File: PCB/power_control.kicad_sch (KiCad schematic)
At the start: 12 parts

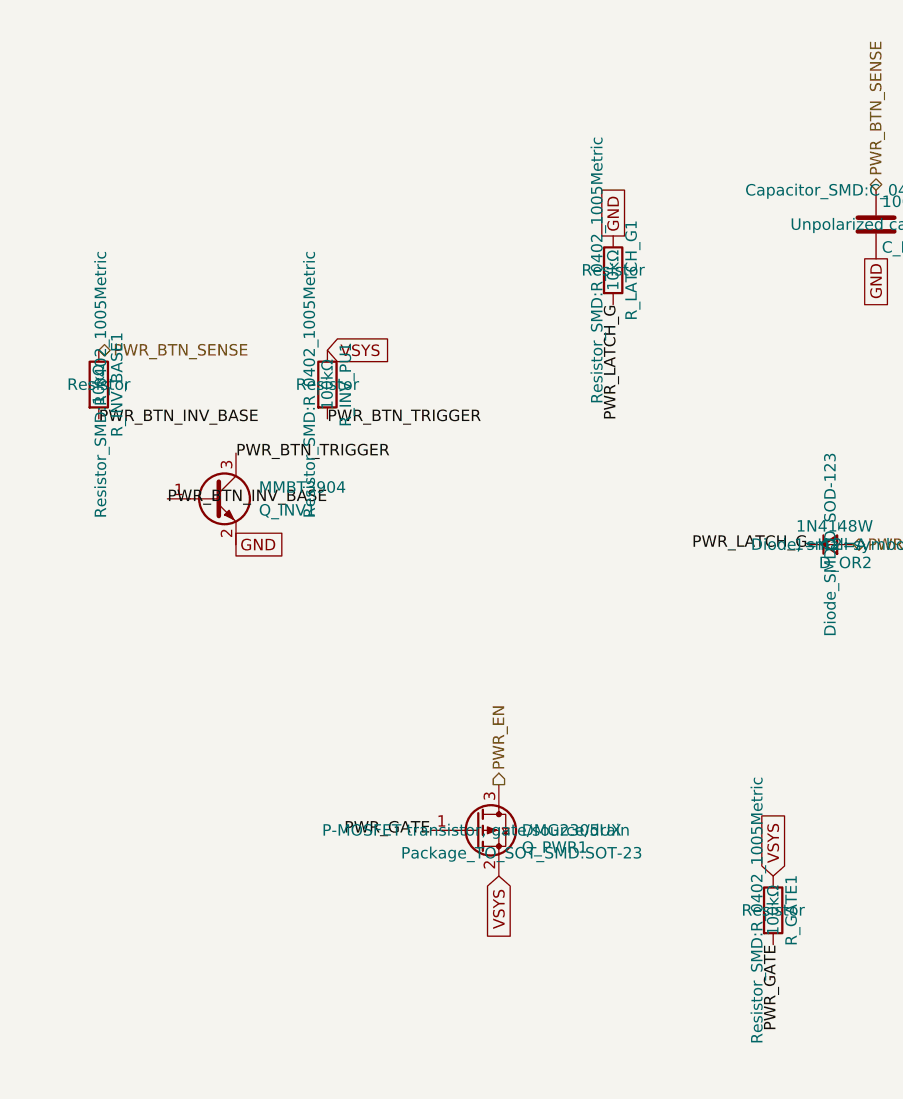
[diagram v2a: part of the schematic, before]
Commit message: fix: latch gate-drive divider, floating buck EN, and missing accelerometer MPNs (#58)
Power latch, round 2 (found via cross-checking a third-party static-analysis
tool run against this project's own netlist and real component datasheets):

- R_LATCH_G1 raised 10kΩ -> 1MΩ. The prior value formed an unintended divider
  with R_INV_PU1 across D_OR1, leaving only ~0.3V at Q_LATCH1's gate on a
  press -- nowhere near enough to turn it on, meaning last round's inverter
  fix likely didn't actually latch on real hardware. Raising the pull-down
  instead of shrinking the pull-up avoids turning Q_INV1's idle state into a
  continuous mA-scale drain.
- R_INV_BASE1 repurposed from a series resistor (which shared current with
  R_BTN_PU1 and sagged the MCU's own button-sense read to ~1V) into its own
  dedicated 100k VSYS pull-up, decoupled via a new Schottky (D_INV_ISO1,
  BAT54W) so a press can still pull the base low without loading the shared
  sense node.
- Added R_PWR_EN_PD1 (100k to GND): the buck's EN pin had no pull-up or
  pull-down at all. TI's TLV62569 datasheet says not to leave it floating;
  Q_PWR1's drain is its only prior connection.

Also fills in MF/MPN for the 4 accelerometer parts (U_ACCEL1, C_ACCEL_1/2/3)
that were missing them, and retires the JLCPCB Basic-library matching
preference -- we're no longer targeting JLCPCB assembly for this board.

power_control_layout diagrams updated to match. Verified via kicad-cli sch
erc, sch export netlist, and pcb drc after every change; production files
regenerated.

Co-authored-by: Claude Sonnet 5 <noreply@anthropic.com>
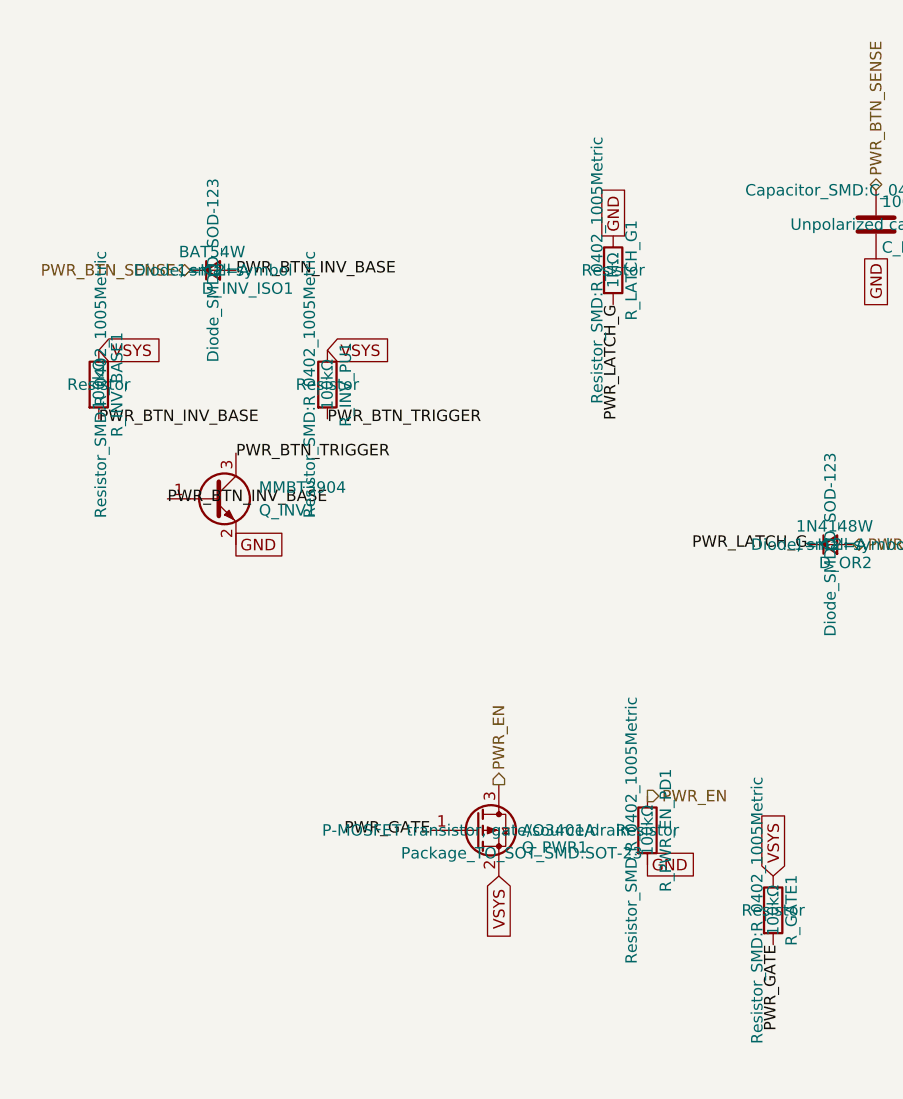
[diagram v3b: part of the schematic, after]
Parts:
- added D_INV_ISO1: BAT54W, Diode_SMD:D_SOD-123, symbol Device:D_Small
- added R_PWR_EN_PD1: 100kΩ, Resistor_SMD:R_0402_1005Metric, symbol Device:R
- Q_PWR1: value DMG2305UX -> AO3401A; LCSC C144153 -> C15127; MF Diodes Incorporated -> Alpha & Omega Semicon; Manufacturer_Part_Number DMG2305UX-13 -> AO3401A
- R_INV_BASE1: value 10kΩ -> 100kΩ; LCSC C25744 -> C25741; Manufacturer_Part_Number 0402WGF1002TCE -> 0402WGF1003TCE
- R_LATCH_G1: value 10kΩ -> 1MΩ; LCSC C25744 -> C26083; Manufacturer_Part_Number 0402WGF1002TCE -> 0402WGF1004TCE
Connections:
- net GND: now also R_PWR_EN_PD1.2
- net PWR_BTN_INV_BASE: now also D_INV_ISO1.2 (A)
- net PWR_BTN_SENSE: now also D_INV_ISO1.1 (K); no longer R_INV_BASE1.1
- net PWR_EN: now also R_PWR_EN_PD1.1
- net VSYS: now also R_INV_BASE1.1

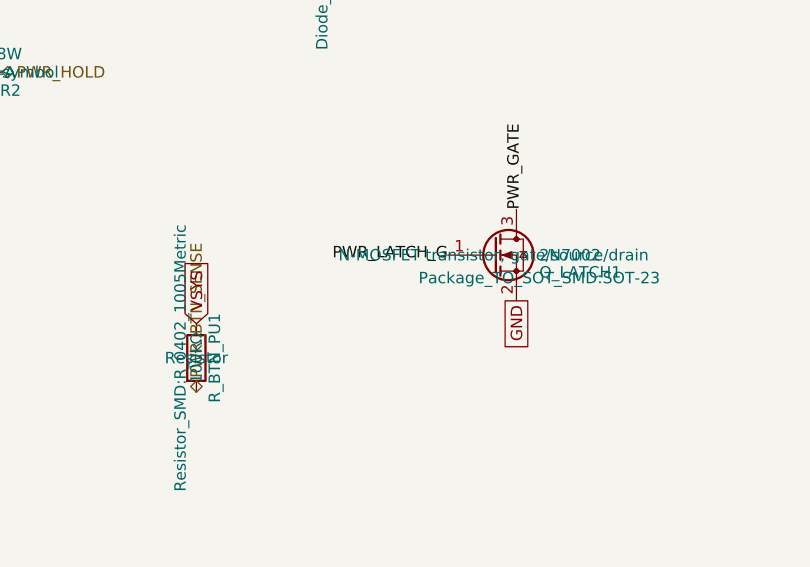
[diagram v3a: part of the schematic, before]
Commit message: fix: keep button-sense within MCU rail, and add latch-gate margin at low battery (#59)
Both found by cross-checking a friend's static-analysis tool against our own
netlist and datasheets.

- R_BTN_PU1 now pulls up to 3V3 instead of VSYS. PWR_BTN_SENSE lands
  directly on GPIO2, whose ceiling is VDD+0.3V (~3.6V), but idled at VSYS
  (up to ~4.5V on USB). It also back-fed the unpowered 3V3 rail through the
  pin's clamp diode when the MCU was off. Safe now that R_INV_BASE1 gives the
  inverter its own VSYS pull-up, so R_BTN_PU1 no longer supplies it. A
  divider can't work across the 3.0-4.5V VSYS range (needs >=2.5V to read
  high but <=3.6V max).
- Q_LATCH1 swapped 2N7002 -> AO3400A. With realistic diode drop the gate
  reaches ~2.4V at VSYS=3.0V, which has no margin against the 2N7002's 2.5V
  worst-case threshold. AO3400A's Vgs(th) max is 1.45V (same SOT-23 G/S/D
  pinout, property-only change, no reroute).

Layout diagrams/docs updated (callouts D and H); production files
regenerated. ERC/DRC clean, all parts have MF/MPN.

Co-authored-by: Claude Sonnet 5 <noreply@anthropic.com>
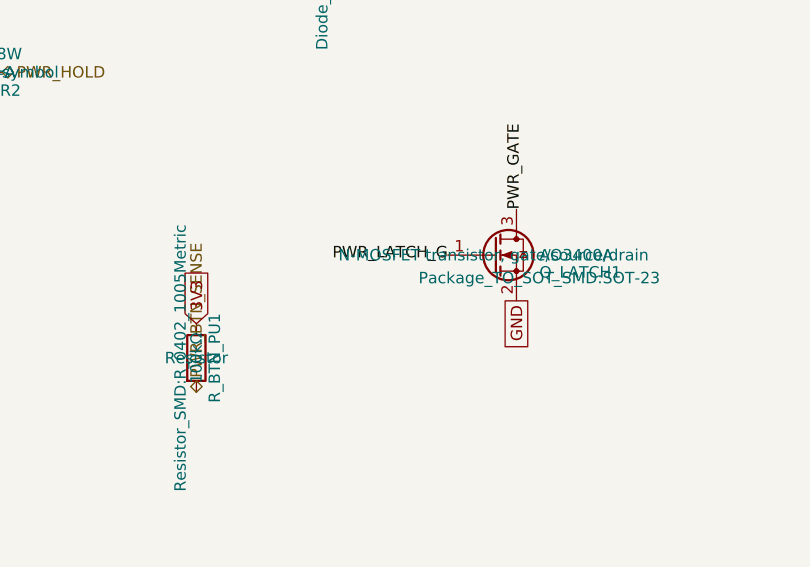
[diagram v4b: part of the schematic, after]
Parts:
- Q_LATCH1: value 2N7002 -> AO3400A; LCSC C8545 -> C20917; MF Jiangsu Changjing Electronics Technology Co., Ltd. -> Alpha & Omega Semicon; Manufacturer_Part_Number 2N7002 -> AO3400A
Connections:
- net VSYS: no longer R_BTN_PU1.1
- new net 3V3: R_BTN_PU1.1
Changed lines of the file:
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@@
 		)
 	)
-	(global_label "VSYS"
+	(global_label "3V3"
 		(shape input)
 		(at 156.21 134.62 90)
@@
 			)
 		)
-		(property "Value" "2N7002"
+		(property "Value" "AO3400A"
 			(at 194.31 127 0)
 			(show_name no)
@@
 			)
 		)
-		(property "MF" "Jiangsu Changjing Electronics Technology Co., Ltd."
-			(at 0 0 0)
-			(hide yes)
-			(show_name no)
-			(do_not_autoplace no)
-			(effects
-				(font
-					(size 1.27 1.27)
-				)
-			)
-		)
-		(property "Manufacturer_Part_Number" "2N7002"
-			(at 0 0 0)
-			(hide yes)
-			(show_name no)
-			(do_not_autoplace no)
-			(effects
-				(font
-					(size 1.27 1.27)
-				)
-			)
-		)
-		(property "LCSC" "C8545"
-			(at 0 0 0)
-			(hide yes)
+		(property "MF" "Alpha & Omega Semicon"
+			(at 0 0 0)
+			(hide yes)
+			(show_name no)
+			(do_not_autoplace no)
+			(effects
+				(font
+					(size 1.27 1.27)
+				)
+			)
+		)
+		(property "Manufacturer_Part_Number" "AO3400A"
+			(at 0 0 0)
+			(hide yes)
+			(show_name no)
+			(do_not_autoplace no)
+			(effects
+				(font
+					(size 1.27 1.27)
+				)
+			)
+		)
+		(property "LCSC" "C20917"
+			(at 0 0 0)
+			(hide yes)

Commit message: fix: add C_LATCH_G1 to stop a ~2ms PWR_EN blip on battery insertion (#60)
* fix: add C_LATCH_G1 to stop a ~2ms PWR_EN blip on battery insertion

There's no physical board yet, so this was found by simulating the
button/inverter/latch circuit in ngspice (KiCad's bundled libngspice) after a
validator run claimed the board would power itself on. That claim doesn't hold
(off-state base sits ~0.6-0.7V because the button node is only grounded
through R_BTN_PU1, and a fast 3V3 collapse at shutdown never lifts the latch
gate), but the simulation did show a real, minor transient: on battery
insertion Q_INV1 isn't conducting until C_DBNC1 charges through D_INV_ISO1, so
PWR_LATCH_G briefly rises to ~VSYS-0.6V and PWR_EN pulses ~1.9ms. This
existed before the 3V3 pull-up change too (~1.4ms).

C_LATCH_G1 (100nF 0402, same part as C_DBNC1) from PWR_LATCH_G to GND slows
the gate rise so the transient peaks at ~0.3V, under the AO3400A's minimum
threshold, at a cost of 4-8ms of press latency. 100nF chosen over 47nF, which
peaked at ~0.65V, right at a minimum-threshold part.

Layout diagrams/docs updated (callout I, routing step 8); production files
regenerated. ERC/DRC clean, all parts have MF/MPN.

Co-Authored-By: Claude Sonnet 5 <noreply@anthropic.com>

* chore: add SPICE check for the power latch, and commit KiCad settings

- scripts/spice/latch_sim.py: ngspice (KiCad's bundled libngspice) check of the
  soft-latch with pass/fail assertions for battery insertion, a press across
  supply/FET-threshold corners, and shutdown. Reproduces the insertion blip
  fixed by C_LATCH_G1 (fails with --cap 0) and the gate-margin reason for
  choosing 100nF over 47nF. README documents what is and isn't modeled.
- PCB/snips_controller.kicad_pro: KiCad's reordered used-designators list.

Co-Authored-By: Claude Sonnet 5 <noreply@anthropic.com>

---------

Co-authored-by: Claude Sonnet 5 <noreply@anthropic.com>
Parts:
- added C_LATCH_G1: 100nF, Capacitor_SMD:C_0402_1005Metric, symbol Device:C
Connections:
- net GND: now also C_LATCH_G1.1
- net PWR_LATCH_G: now also C_LATCH_G1.2
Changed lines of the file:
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@@
+		)
+	)
+	(global_label "GND"
+		(shape passive)
+		(at 115.57 72.39 90)
+		(fields_autoplaced yes)
+		(effects
+			(font
+				(size 1.27 1.27)
+			)
+			(justify left)
+		)
+		(property "Intersheetrefs" "${INTERSHEET_REFS}"
+			(at 115.57 72.39 0)
+			(hide yes)
+			(show_name no)
+			(do_not_autoplace no)
+			(effects
+				(font
+					(size 1.27 1.27)
+				)
+			)
+		)
+	)
+	(label "PWR_LATCH_G"
+		(at 115.57 80.01 270)
+		(effects
+			(font
+				(size 1.27 1.27)
+			)
+			(justify right)
+		)
+	)
+	(symbol
+		(lib_id "Device:C")
+		(at 115.57 76.2 0)
+		(unit 1)
+		(body_style 1)
+		(exclude_from_sim no)
+		(in_bom yes)
+		(on_board yes)
+		(in_pos_files yes)
+		(dnp no)
+		(fields_autoplaced yes)
+		(property "Reference" "C_LATCH_G1"
+			(at 116.205 78.74 0)
+			(show_name no)
+			(do_not_autoplace no)
+			(effects
+				(font
+					(size 1.27 1.27)
+				)
+				(justify left)
+			)
+		)
+		(property "Value" "100nF"
+			(at 116.205 73.66 0)
+			(show_name no)
+			(do_not_autoplace no)
+			(effects
+				(font
+					(size 1.27 1.27)
+				)
+				(justify left)
+			)
+		)
+		(property "Footprint" "Capacitor_SMD:C_0402_1005Metric"
+			(at 116.5352 72.39 0)
+			(show_name no)
+			(do_not_autoplace no)
+			(effects
+				(font
+					(size 1.27 1.27)
+				)
+			)
+		)
+		(property "Datasheet" ""
+			(at 115.57 76.2 0)
+			(show_name no)
+			(do_not_autoplace no)
+			(effects
+				(font
+					(size 1.27 1.27)
+				)
+			)
+		)
+		(property "Description" "Unpolarized capacitor"
+			(at 115.57 76.2 0)
+			(show_name no)
+			(do_not_autoplace no)
+			(effects
+				(font
+					(size 1.27 1.27)
+				)
+			)
+		)
+		(property "MF" "Samsung Electro-Mechanics"
+			(at 0 0 0)
+			(hide yes)
+			(show_name no)
+			(do_not_autoplace no)
+			(effects
+				(font
+					(size 1.27 1.27)
+				)
+			)
+		)
+		(property "Manufacturer_Part_Number" "CL05B104KO5NNNC"
+			(at 0 0 0)
+			(hide yes)
+			(show_name no)
+			(do_not_autoplace no)
+			(effects
+				(font
+					(size 1.27 1.27)
+				)
+			)
+		)
+		(property "LCSC" "C1525"
+			(at 0 0 0)
+			(hide yes)
+			(show_name no)
+			(do_not_autoplace no)
+			(effects
+				(font
+					(size 1.27 1.27)
+				)
+			)
+		)
+		(pin "1"
+		)
+		(pin "2"
+		)
+		(instances
+			(project "snips_controller"
+				(path "/21935953-32a0-46ad-8079-8177920c6978/081a4841-1e21-4908-a8a8-37f54f8809f6"
+					(reference "C_LATCH_G1")
+					(unit 1)
+				)
+			)
 		)
 	)
